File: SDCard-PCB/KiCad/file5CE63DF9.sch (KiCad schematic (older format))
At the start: 18 parts, among them J10 Conn_01x01, J11 Conn_01x01, J12 Conn_01x01, J13 Conn_01x01, J18 Conn_01x01, J19 Conn_01x01, J2 Conn_01x01, J20 Conn_01x01, J21 Conn_01x01, J28 Conn_01x01, J3 Conn_01x01, J4 Conn_01x01, J5 Conn_01x01, J9 Conn_01x01, U1 MAX13030EETE+

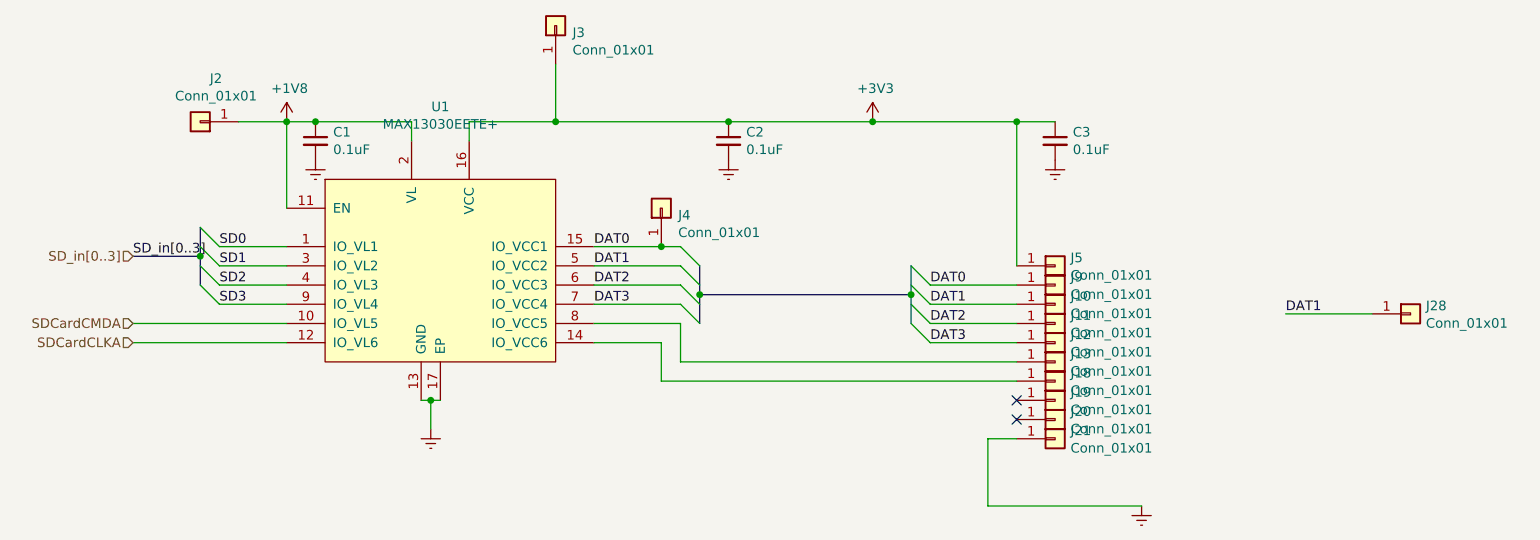
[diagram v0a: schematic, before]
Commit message: Finish schematics, begin PCB design
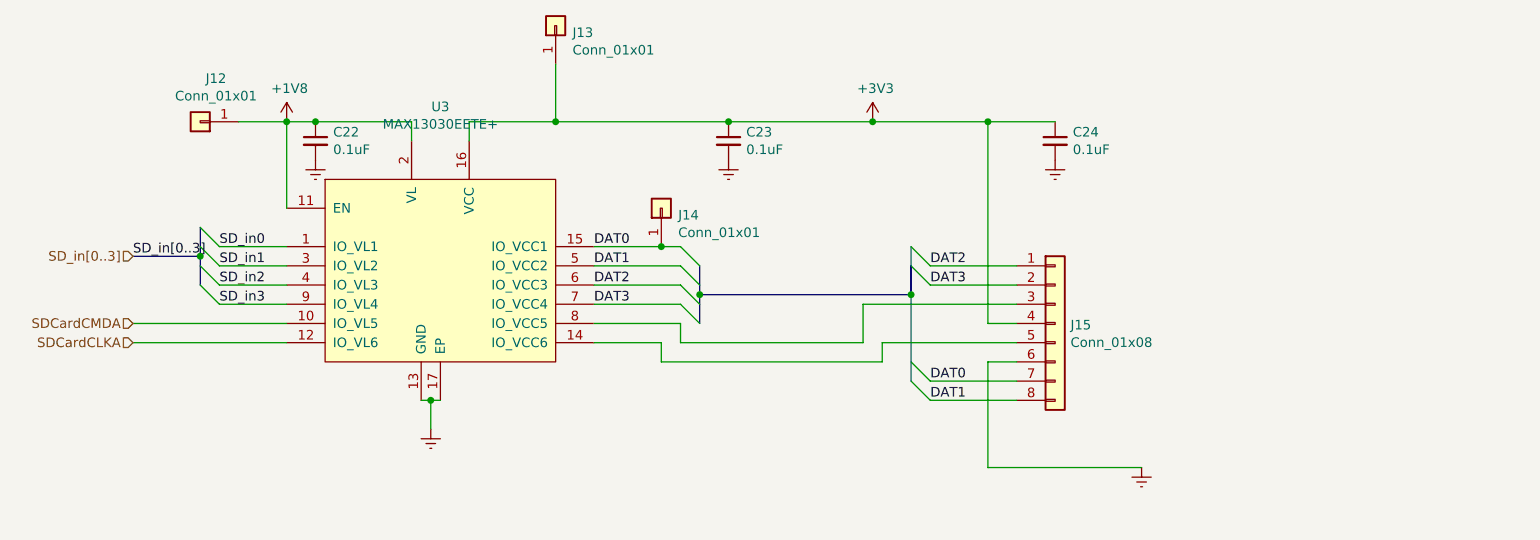
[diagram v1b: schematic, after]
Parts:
- removed J10, J11, J12, J13, J18, J19, J20, J21, J5, J9: Conn_01x01, symbol .Connector:Conn_01x01
- removed J28: Conn_01x01, .Connector:Conn_1x1_700_Circular_Pad, symbol .Connector:Conn_01x01
- added J15: Conn_01x08, .Connector:1x8_microSD, symbol Connector_Generic:Conn_01x08
- renumbered C1 to C22, C2 to C23, C3 to C24, J2 to J12, J3 to J13, J4 to J14, U1 to U3
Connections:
- net +3V3: now also J15.4 (Pin_4)
- net DAT0: now also J15.7 (Pin_7)
- net DAT1: now also J15.8 (Pin_8)
- net DAT2: now also J15.1 (Pin_1)
- net DAT3: now also J15.2 (Pin_2)
- net Earth: now also J15.6 (Pin_6)
- net at U3.14 (IO_VCC6): now also J15.5 (Pin_5)
- net at U3.8 (IO_VCC5): now also J15.3 (Pin_3)
- net SD0 renamed SD_in0
- net SD1 renamed SD_in1
- net SD2 renamed SD_in2
- net SD3 renamed SD_in3
- no-connect marks 2 -> 0

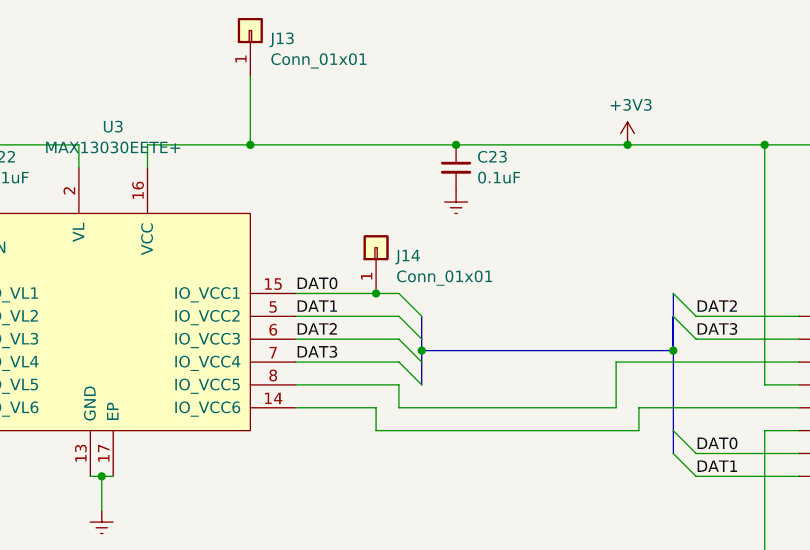
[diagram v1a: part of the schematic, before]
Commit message: PlugIn PCB Ready
1. Completes the PCBNew drawing for MicroSD PlugIn PCB
2. Passes the DRC rule check
3. Generate Gerber files
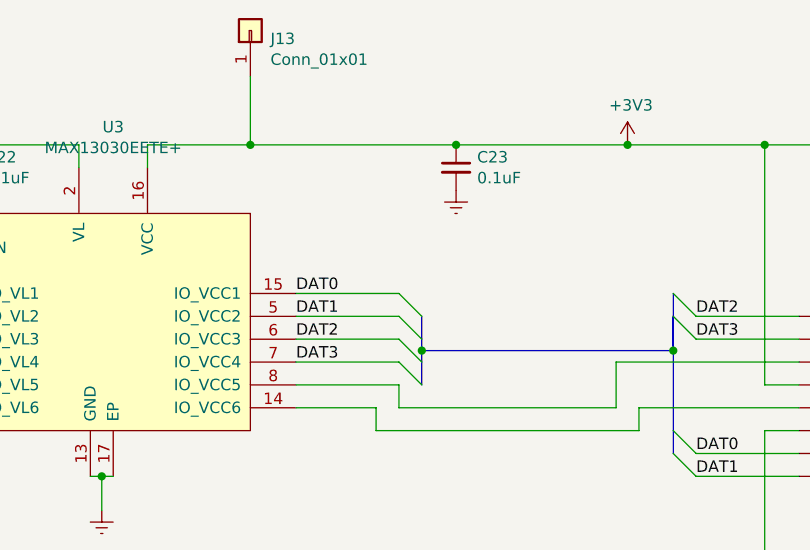
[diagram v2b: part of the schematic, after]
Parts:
- removed J14: Conn_01x01, .Connector:Conn_1x1_700_Circular_Pad, symbol .Connector:Conn_01x01
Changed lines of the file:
@@
 $EndComp
-Wire Wire Line
-	5500 2850 5850 2850
 Wire Wire Line
 	5500 2950 5950 2950
@@
 	0    -1   -1   0
 $EndComp
-$Comp
-L .Connector:Conn_01x01 J14
-U 1 1 5CB2578C
-P 5850 2650
-F 0 "J14" V 5814 2562 50  0000 R CNN
-F 1 "Conn_01x01" V 5723 2562 50  0000 R CNN
-F 2 ".Connector:Conn_1x1_700_Circular_Pad" H 5850 2650 50  0001 C CNN
-F 3 "~" H 5850 2650 50  0001 C CNN
-	1    5850 2650
-	0    -1   -1   0
-$EndComp
-Connection ~ 5850 2850
-Wire Wire Line
-	5850 2850 5950 2850
 Wire Wire Line
 	7550 4000 8350 4000
@@
 Wire Wire Line
 	7550 3250 7550 2200
+Connection ~ 7550 2200
+Wire Wire Line
+	7550 2200 7900 2200
 Wire Bus Line
 	7150 2950 7150 3100
@@
 Wire Bus Line
 	7150 3100 7150 3550
-Connection ~ 7550 2200
-Wire Wire Line
-	7550 2200 7900 2200
+Wire Wire Line
+	5500 2850 5950 2850
 $EndSCHEMATC
